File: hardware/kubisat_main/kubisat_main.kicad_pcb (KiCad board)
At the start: 2 copper layers, 80 x 80 mm, 55 parts, among them J1 IPX, J2 Micro_SD_Card_Det1, J3 Conn_01x06_MountingPin, SW1 BOOTSEL, SW2 RESET, U1 RP2040, U2 NEO-6M-GPS, U3 MPU-6050, U4 MMC5883MA, U6 W25Q16JVSS, U6 XL1278-SMT, U7 BME280, U8 DS3231M, Y1 12MHz

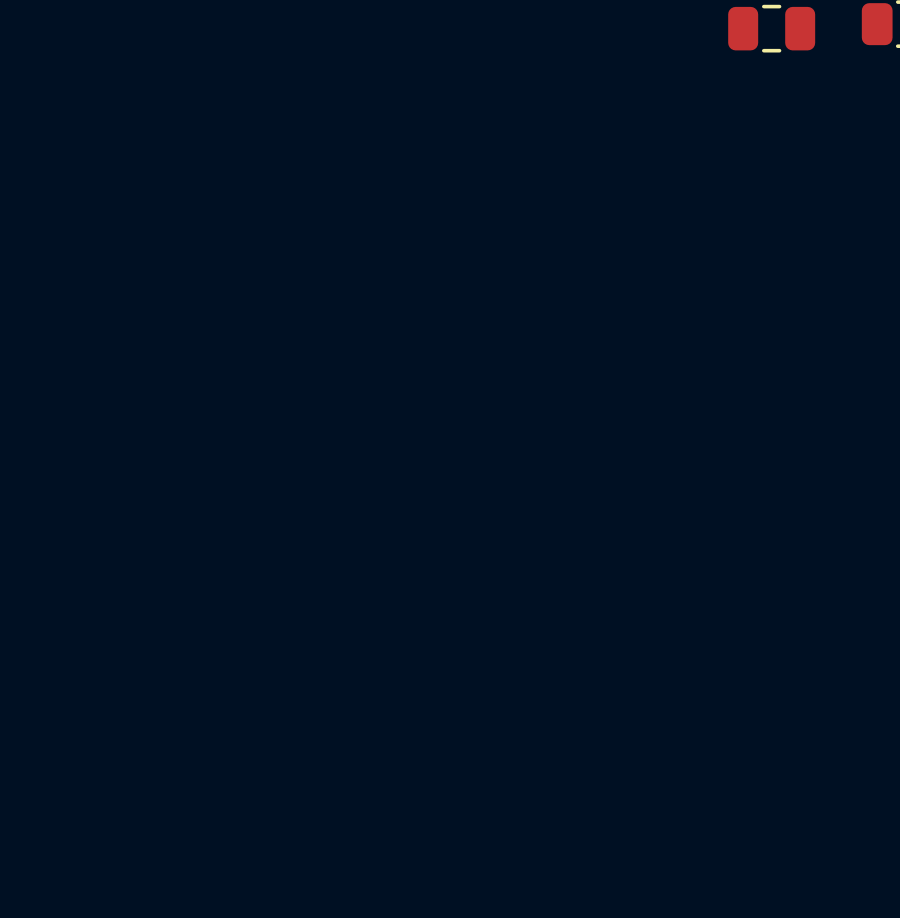
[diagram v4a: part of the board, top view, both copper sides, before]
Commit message: added pcb elements
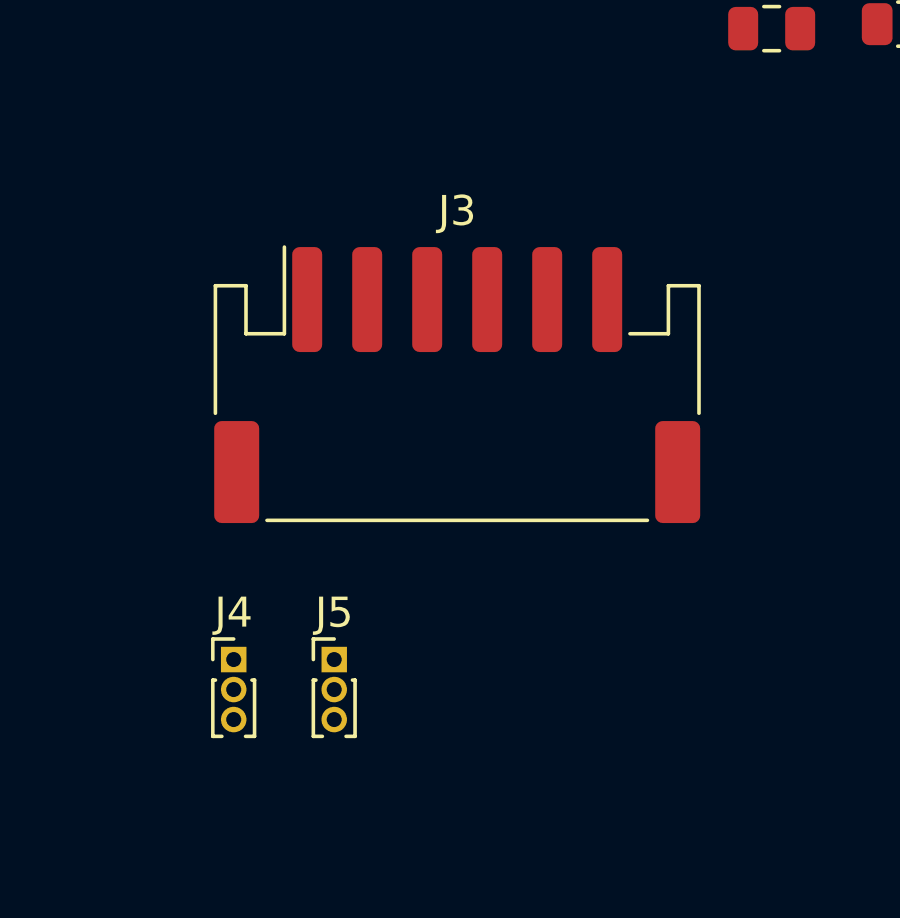
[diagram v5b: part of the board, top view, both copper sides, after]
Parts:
- added J3: Conn_01x06_MountingPin, Connector_JST:JST_PH_S6B-PH-SM4-TB_1x06-1MP_P2.00mm_Horizontal, F.Cu at (47.0, 74.2)
- added J4: DEBUG_SWD, Connector_PinHeader_1.00mm:PinHeader_1x03_P1.00mm_Vertical, F.Cu at (39.5, 83.4)
- added J5: UART0, Connector_PinHeader_1.00mm:PinHeader_1x03_P1.00mm_Vertical, F.Cu at (42.9, 83.4)
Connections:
- U1 pad 2: UART0_TX -> Net-(J5-Pin_3)
- U1 pad 24: unconnected-(U1-SWCLK-Pad24) -> Net-(J4-Pin_1)
- U1 pad 25: unconnected-(U1-SWD-Pad25) -> Net-(J4-Pin_3)
- U1 pad 3: UART0_RX -> Net-(J5-Pin_1)

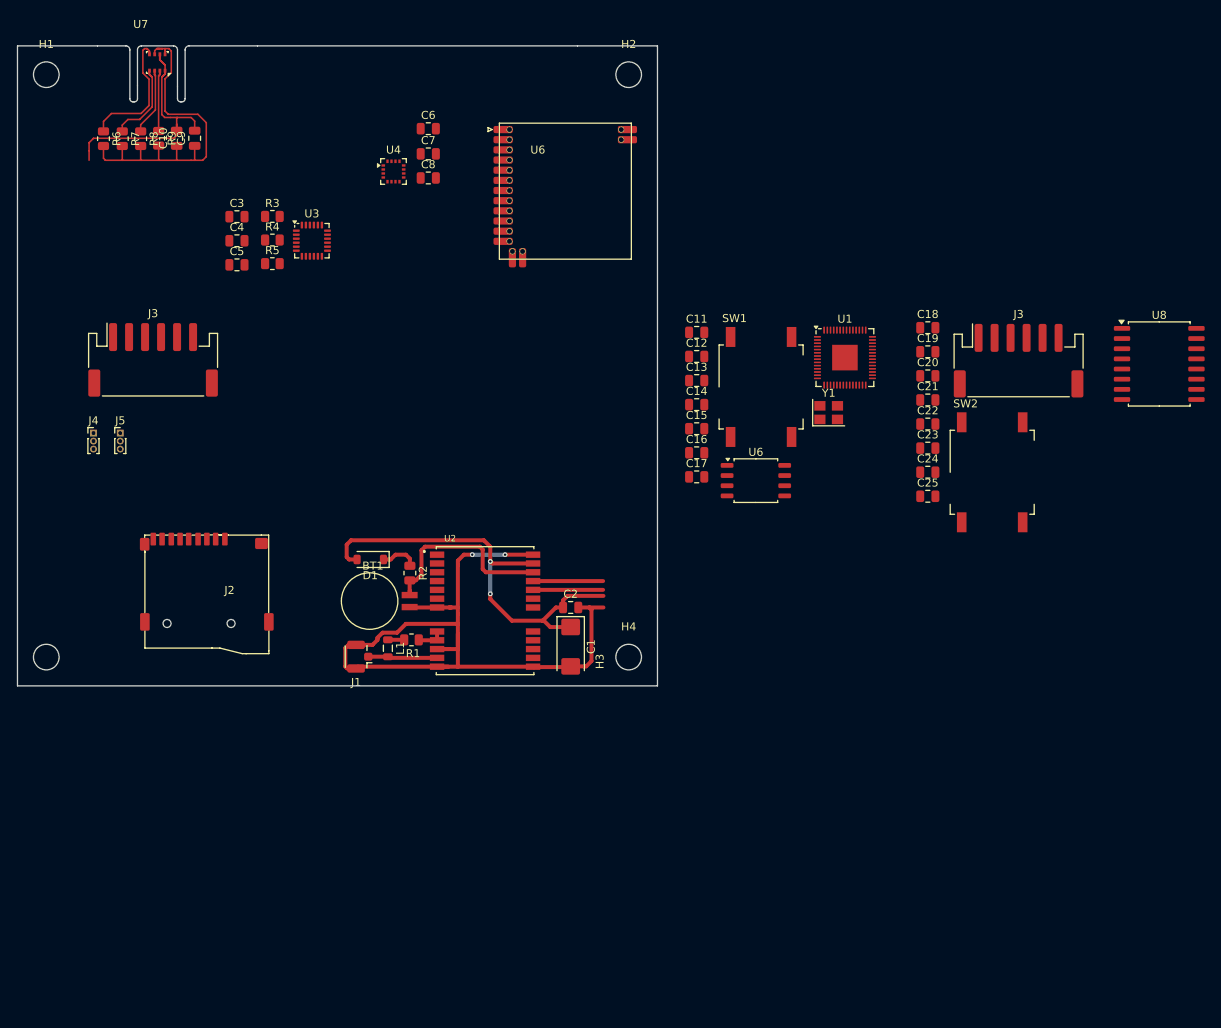
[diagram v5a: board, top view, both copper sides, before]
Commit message: changed strucutre, split main into 2 sseparate boards
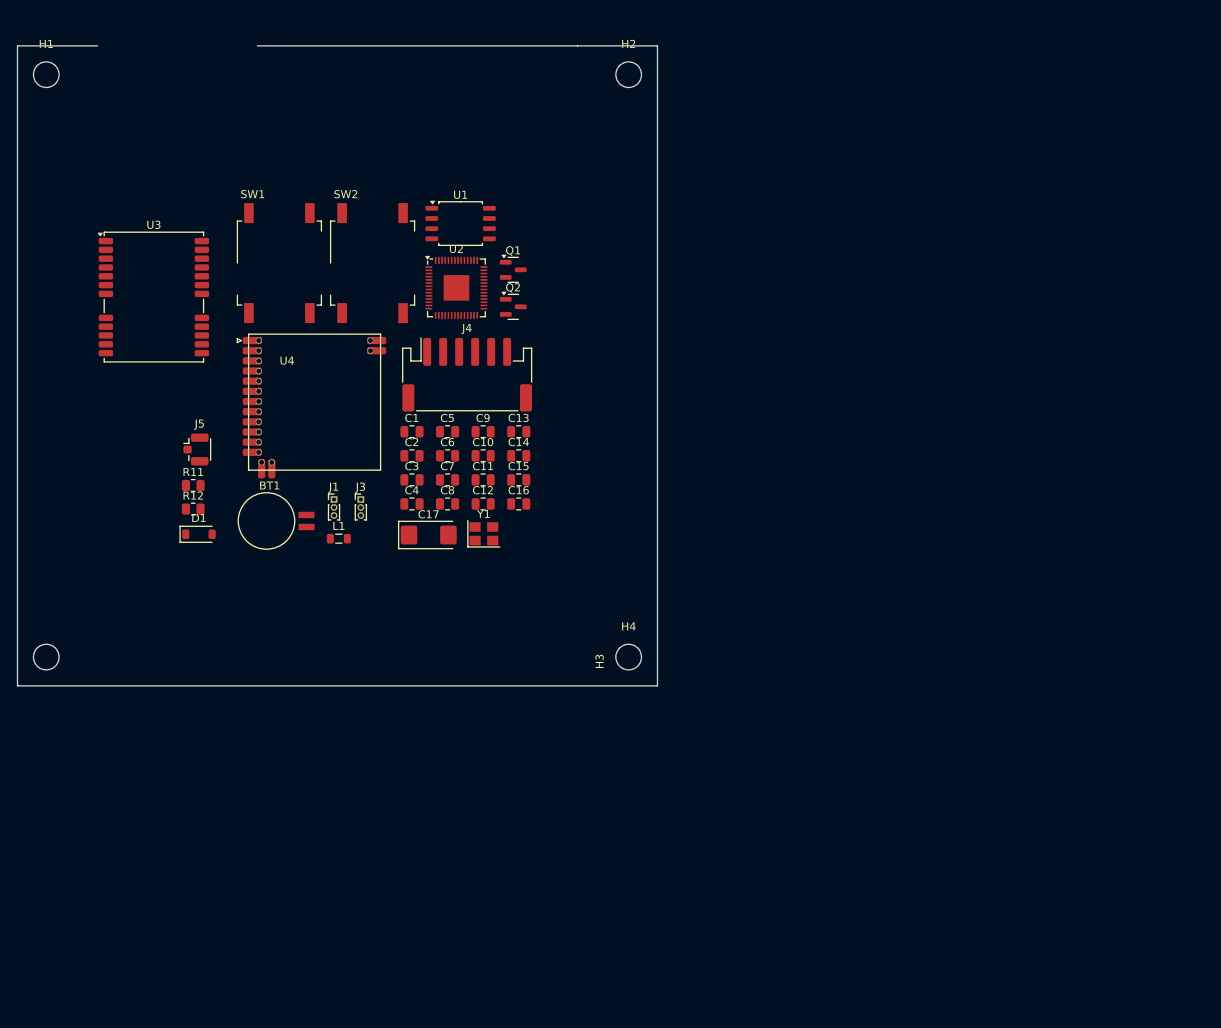
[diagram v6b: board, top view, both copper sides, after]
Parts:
- removed C18, C19, C20, C21, C22, C23, C24, C25: 100n, Capacitor_SMD:C_0805_2012Metric
- removed J2: Micro_SD_Card_Det1, Connector_Card:MR01A-01211
- removed the J3 at (155.1, 74.3)
- removed the J3 at (47.0, 74.2)
- removed R1: 22, Resistor_SMD:R_0805_2012Metric
- removed R2: 1k, Resistor_SMD:R_0805_2012Metric
- removed R3, R4, R5: 4k7, Resistor_SMD:R_0805_2012Metric
- removed R6, R7, R8, R9: 10k, Resistor_SMD:R_0805_2012Metric
- removed U6: W25Q16JVSS, Package_SO:SOIC-8_5.23x5.23mm_P1.27mm
- removed U6: XL1278-SMT, RF:XL1278-SMT
- removed U7: BME280, Package_LGA:Bosch_LGA-8_2.5x2.5mm_P0.65mm_ClockwisePinNumbering
- removed U8: DS3231M, Package_SO:SOIC-16W_7.5x10.3mm_P1.27mm
- added J3: UART0, Connector_PinHeader_1.00mm:PinHeader_1x03_P1.00mm_Vertical, F.Cu at (72.9, 91.7)
- added Q1: BSS138, Package_TO_SOT_SMD:SOT-23, F.Cu at (92.0, 63.0)
- added Q2: BSS138, Package_TO_SOT_SMD:SOT-23, F.Cu at (92.0, 67.6)
- added R11: 22, Resistor_SMD:R_0805_2012Metric, F.Cu at (52.0, 90.0)
- added R12: 1k, Resistor_SMD:R_0805_2012Metric, F.Cu at (52.0, 92.9)
- C1: value 220u/10V -> 100n; footprint Capacitor_Tantalum_SMD:CP_EIA-6032-15_Kemet-U -> Capacitor_SMD:C_0805_2012Metric
- C10: value 1u -> 100n
- C13: value 2u2 -> 100n
- C16: value 15p -> 100n
- C17: value 15p -> 220u/10V; footprint Capacitor_SMD:C_0805_2012Metric -> Capacitor_Tantalum_SMD:CP_EIA-6032-15_Kemet-U
- C4: value 10n -> 100n
- C5: value 2n2 -> 2u2
- C6: value 100n -> 15p
- C7: value 4u7 -> 15p
- C8: value 200n -> 100n
- J1: value IPX -> DEBUG_SWD; footprint Connector_Coaxial:U.FL_Hirose_U.FL-R-SMT-1_Vertical -> Connector_PinHeader_1.00mm:PinHeader_1x03_P1.00mm_Vertical
- J4: value DEBUG_SWD -> POWER_IN; footprint Connector_PinHeader_1.00mm:PinHeader_1x03_P1.00mm_Vertical -> Connector_JST:JST_PH_S6B-PH-SM4-TB_1x06-1MP_P2.00mm_Horizontal
- J5: value UART0 -> IPX; footprint Connector_PinHeader_1.00mm:PinHeader_1x03_P1.00mm_Vertical -> Connector_Coaxial:U.FL_Hirose_U.FL-R-SMT-1_Vertical
- U1: value RP2040 -> W25Q16JVSS; footprint Package_DFN_QFN:QFN-56-1EP_7x7mm_P0.4mm_EP3.2x3.2mm -> Package_SO:SOIC-8_5.23x5.23mm_P1.27mm
- U2: value NEO-6M-GPS -> RP2040; footprint RF_GPS:XCVR_NEO-6M-GPS -> Package_DFN_QFN:QFN-56-1EP_7x7mm_P0.4mm_EP3.2x3.2mm
- U3: value MPU-6050 -> NEO-6M-GPS; footprint Sensor_Motion:InvenSense_QFN-24_4x4mm_P0.5mm -> RF_GPS:ublox_NEO
- U4: value MMC5883MA -> XL1278-SMT; footprint Package_LGA:LGA-16_3x3mm_P0.5mm -> RF:XL1278-SMT
- moved SW2 81.7 mm to (74.4, 62.1)
- moved SW1 62.2 mm to (62.7, 62.1)
- moved C10 55.2 mm to (88.2, 86.2), turned to 0 degrees
- moved C9 51.4 mm to (88.2, 83.2), turned to 0 degrees
- moved U1 50.9 mm to (85.4, 57.2)
- moved J4 47.3 mm to (86.2, 76.1)
- moved Y1 45.7 mm to (88.3, 96.0)
- moved C6 41.0 mm to (83.8, 86.2)
- moved C8 40.8 mm to (83.8, 92.3)
- moved C7 40.8 mm to (83.8, 89.2)
- moved U2 40.5 mm to (84.9, 65.2)
- moved C3 39.5 mm to (79.3, 89.2)
- moved C4 39.5 mm to (79.3, 92.3)
- moved C17 34.3 mm to (81.4, 96.1)
- moved C5 33.6 mm to (83.8, 83.2)
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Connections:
- C1 pad 1: +3V3 -> GND
- C1 pad 2: GND -> +3V3
- C11 pad 1: +1V1 -> +3V3
- C12 pad 1: GND -> +3V3
- C12 pad 2: +1V1 -> GND
- C13 pad 1: GND -> +3V3
- C13 pad 2: Net-(U1-ADC_AVDD) -> GND
- C14 pad 1: GND -> +3V3
- C14 pad 2: +3V3 -> GND
- C15 pad 2: +3V3 -> Net-(U2-ADC_AVDD)
- C16 pad 1: GND -> +3V3
- C16 pad 2: Net-(U1-XIN) -> GND
- C17 pad 1: GND -> +3V3
- C17 pad 2: Net-(C17-Pad2) -> GND
- C2 pad 1: +3V3 -> +1V1
- C3 pad 2: Net-(U3-REGOUT) -> +1V1
- C4 pad 1: +3V3 -> GND
- C4 pad 2: GND -> +1V1
- C5 pad 1: Net-(U3-CPOUT) -> GND
- C5 pad 2: GND -> +3V3
- C6 pad 1: +3V3 -> GND
- C6 pad 2: GND -> Net-(U2-XIN)
- C7 pad 1: unconnected-(C7-Pad1) -> GND
- C7 pad 2: GND -> Net-(C7-Pad2)
- C8 pad 1: unconnected-(C8-Pad1) -> +3V3
- C8 pad 2: unconnected-(C8-Pad2) -> GND
- J1 pad 1: RF_IN -> Net-(J1-Pin_1)
- J4 pad 1: Net-(J4-Pin_1) -> GND
- J4 pad 3: Net-(J4-Pin_3) -> /NC
- J5 pad 1: Net-(J5-Pin_1) -> RF_IN
- SW2 pad 2: Net-(U1-RUN) -> Net-(U2-RUN)
- U1 pad 1: +3V3 -> Net-(U1-~{CS})
- U1 pad 2: Net-(J5-Pin_3) -> Net-(U1-DO(IO1))
- U1 pad 3: Net-(J5-Pin_1) -> Net-(U1-IO2)
- U1 pad 4: unconnected-(U1-GPIO2-Pad4) -> GND
- U1 pad 5: unconnected-(U1-GPIO3-Pad5) -> Net-(U1-DI(IO0))
- U1 pad 6: I2C0_SDA -> Net-(U1-CLK)
- U1 pad 7: I2C0_SCL -> Net-(U1-IO3)
- U1 pad 8: unconnected-(U1-GPIO6-Pad8) -> +3V3
- U2 pad 1: (no net) -> +3V3
- U2 pad 10: GND -> +3V3
- U2 pad 11: RF_IN -> SD.MISO
- U2 pad 12: GND -> SD.CS
- U2 pad 13: GND -> SD.CLK
- U2 pad 14: unconnected-(U2-MOSI/CFG_COM0-Pad14) -> SD.MOSI
- U2 pad 16: unconnected-(U2-CFG_GPS0/SCK-Pad16) -> SX1278.DIO1
- U2 pad 17: unconnected-(U2-RSVD_17-Pad17) -> SX1278.DIO0
- U2 pad 18: unconnected-(U2-SDA2-Pad18) -> SX1278.RES
- U2 pad 19: unconnected-(U2-SCL2-Pad19) -> GND
- U2 pad 2: unconnected-(U2-SS_N-Pad2) -> Net-(J3-Pin_3)
- U2 pad 20: unconnected-(U2-TXD1-Pad20) -> Net-(U2-XIN)
- U2 pad 21: unconnected-(U2-RXD1-Pad21) -> Net-(U2-XOUT)
- U2 pad 22: Net-(BT1-+) -> +3V3
- U2 pad 23: +3V3 -> +1V1
- U2 pad 24: GND -> Net-(J1-Pin_1)
- U2 pad 3: unconnected-(U2-TIMEPULSE-Pad3) -> Net-(J3-Pin_1)
- U2 pad 6: unconnected-(U2-USB_DP-Pad6) -> I2C0_SDA
- U2 pad 7: GND -> I2C0_SCL
- U2 pad 8: Net-(U2-RSVD_8) -> unconnected-(U2-GPIO6-Pad8)
- U2 pad 9: Net-(U2-RSVD_8) -> unconnected-(U2-GPIO7-Pad9)
- U3 pad 1: GND -> (no net)
- U3 pad 10: Net-(U3-REGOUT) -> GND
- U3 pad 11: GND -> RF_IN
- U3 pad 12: unconnected-(U3-INT-Pad12) -> GND
- U3 pad 13: +3V3 -> GND
- U3 pad 18: GND -> unconnected-(U3-SDA2-Pad18)
- U3 pad 20: Net-(U3-CPOUT) -> GPS_TX
- U3 pad 21: unconnected-(U3-RESV-Pad21) -> GPS_RX
- U3 pad 22: unconnected-(U3-RESV-Pad22) -> Net-(BT1-+)
- U3 pad 23: SCL -> +3V3
- U3 pad 24: SDA -> GND
- U3 pad 7: unconnected-(U3-AUX_CL-Pad7) -> GND
- U3 pad 8: +3V3 -> Net-(U3-RSVD_8)
- U3 pad 9: Net-(U3-AD0) -> Net-(U3-RSVD_8)
- U4 pad 1: unconnected-(U4-SCL-Pad1) -> GND
- U4 pad 10: unconnected-(U4-CAP-Pad10) -> /DIO0
- U4 pad 11: Net-(U4-GND-Pad11) -> /RES
- U4 pad 12: unconnected-(U4-NC-Pad12) -> GND
- U4 pad 16: unconnected-(U4-SDA-Pad16) -> Net-(AE1-A)
- U4 pad 2: unconnected-(U4-VDD-Pad2) -> /DIO1
- U4 pad 5: unconnected-(U4-NC-Pad5) -> SX1278_VCC
- U4 pad 6: unconnected-(U4-NC-Pad6) -> /MISO
- U4 pad 7: unconnected-(U4-NC-Pad7) -> /MOSI
- U4 pad 8: unconnected-(U4-NC-Pad8) -> /SCLK
- U4 pad 9: Net-(U4-GND-Pad11) -> /NSS
- Y1 pad 1: Net-(U1-XIN) -> Net-(U2-XIN)
- Y1 pad 3: Net-(C17-Pad2) -> Net-(C7-Pad2)
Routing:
- net GND: track 128.3 -> 0.00 mm, vias 2 -> 0
- net +3V3: track 101.4 -> 0.00 mm, vias 2 -> 0
- net Net-(BT1-+): track 23.6 -> 0.00 mm
- net Net-(U7-SDO): track 17.3 -> 0.00 mm
- net SCL: track 11.2 -> 0.00 mm
- net SDA: track 9.11 -> 0.00 mm
- net unconnected-(U2-TXD1-Pad20): track 8.75 -> 0.00 mm
- net unconnected-(U2-RXD1-Pad21): track 8.75 -> 0.00 mm
- net RF_IN: track 8.66 -> 0.00 mm
- net Net-(U7-CSB): track 8.39 -> 0.00 mm
- net Net-(D1-K): track 4.64 -> 0.00 mm
- net Net-(U2-RSVD_8): track 3.15 -> 0.00 mm
- net Net-(L1-Pad1): track 2.04 -> 0.00 mm
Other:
- outline, holes or cut-outs redrawn

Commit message: completed (?) mainboard schematic
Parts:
- removed C10, C11, C12, C13, C14, C3, C4, C8, C9: 100n, Capacitor_SMD:C_0805_2012Metric
- removed C15, C5: 2u2, Capacitor_SMD:C_0805_2012Metric
- removed C6, C7: 15p, Capacitor_SMD:C_0805_2012Metric
- removed D1: 1N5817, Diode_SMD:D_SOD-123
- removed R12: 1k, Resistor_SMD:R_0805_2012Metric
- removed SW1: BOOTSEL, Button_Switch_SMD:SW_MEC_5GSH9
- removed U2: RP2040, Package_DFN_QFN:QFN-56-1EP_7x7mm_P0.4mm_EP3.2x3.2mm
- removed Y1: 12MHz, Crystal:Crystal_SMD_3225-4Pin_3.2x2.5mm
- added J2: Micro_SD_Card_Det1, Connector_Card:J_SD_Card-micro_socket_A, F.Cu at (68.7, 44.7)
- added J6: POWER, Connector_JST:JST_PH_B3B-PH-SM4-TB_1x03-1MP_P2.00mm_Vertical, F.Cu at (45.0, 110.7)
- added J7: I2C1, Connector_JST:JST_PH_B2B-PH-SM4-TB_1x02-1MP_P2.00mm_Vertical, F.Cu at (56.9, 110.8)
- added J8: SPI0, Connector_JST:JST_PH_B4B-PH-SM4-TB_1x04-1MP_P2.00mm_Vertical, F.Cu at (36.3, 97.1)
- added JP1: ECO, Jumper:SolderJumper-2_P1.3mm_Open_RoundedPad1.0x1.5mm, F.Cu at (59.5, 89.0)
- added R1: 4k7, Resistor_SMD:R_0805_2012Metric, F.Cu at (70.1, 76.7)
- added R10: 10k, Resistor_SMD:R_0805_2012Metric, F.Cu at (66.5, 102.0)
- added R2: 4k7, Resistor_SMD:R_0805_2012Metric, F.Cu at (65.5, 77.0)
- added R3: 4k7, Resistor_SMD:R_0805_2012Metric, F.Cu at (64.8, 56.9)
- added R4: 4k7, Resistor_SMD:R_0805_2012Metric, F.Cu at (67.7, 56.9)
- added R5: 4k7, Resistor_SMD:R_0805_2012Metric, F.Cu at (70.7, 56.9)
- added R6: 4k7, Resistor_SMD:R_0805_2012Metric, F.Cu at (73.6, 56.9)
- added R7: 10k, Resistor_SMD:R_0805_2012Metric, F.Cu at (75.3, 102.0)
- added R8: 10k, Resistor_SMD:R_0805_2012Metric, F.Cu at (72.4, 102.0)
- added R9: 10k, Resistor_SMD:R_0805_2012Metric, F.Cu at (69.5, 102.0)
- added U5: ~, Package_TO_SOT_SMD:SOT-23-5, F.Cu at (47.4, 92.1)
- added U6: Pico, KiCadLibraries:RPi_Pico_SMD_TH, F.Cu at (90.0, 62.2)
- BT1: value Battery_Cell -> LIR2023; footprint Battery:BatteryHolder_Seiko_MS621F -> Battery:BatteryHolder_Keystone_106_1x20mm
- C1, C2: value 100n -> 10u; footprint Capacitor_SMD:C_0805_2012Metric -> Capacitor_Tantalum_SMD:CP_EIA-3216-18_Kemet-A
- SW2: footprint Button_Switch_SMD:SW_MEC_5GSH9 -> Button_Switch_SMD:SW_SPST_B3SL-1002P
- U1: value W25Q16JVSS -> DS3231M; footprint Package_SO:SOIC-8_5.23x5.23mm_P1.27mm -> Package_SO:SOIC-16W_7.5x10.3mm_P1.27mm
- moved BT1 59.8 mm to (45.1, 38.4), turned to -90 degrees
- moved U4 47.9 mm to (100.8, 97.0), turned to -90 degrees
- moved J1 45.2 mm to (107.7, 67.5)
- moved J3 38.9 mm to (107.5, 73.8)
- moved Q1 38.7 mm to (74.0, 97.2), turned to -90 degrees
- moved Q2 37.2 mm to (69.3, 97.2), turned to -90 degrees
- moved J4 36.6 mm to (71.2, 109.5)
- moved SW2 35.3 mm to (109.3, 56.5), turned to -90 degrees
- moved C16 35.3 mm to (57.4, 93.1)
- moved C1 27.0 mm to (56.2, 97.1)
- moved C17 25.5 mm to (59.4, 83.2)
- moved U1 20.5 mm to (67.5, 67.2)
- moved L1 20.1 mm to (53.1, 86.0)
- moved C2 18.2 mm to (62.3, 92.6)
- moved U3 14.6 mm to (41.0, 79.7)
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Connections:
- BT1 pad 1: Net-(BT1-+) -> 3V_BACKUP
- C1 pad 1: GND -> +5V
- C1 pad 2: +3V3 -> GND
- C2 pad 1: +1V1 -> 3V3_GPS
- J3 pad 2: GND -> Net-(J3-Pin_2)
- J3 pad 3: Net-(J3-Pin_3) -> GND
- J4 pad 4: 5VIN -> +5V
- Q1 pad 1: 3V3 -> +3.3V
- Q1 pad 2: I2C0_SCL -> I2C1_SCL
- Q2 pad 1: 3V3 -> +3.3V
- Q2 pad 2: I2C0_SDA -> I2C1_SDA
- SW2 pad 1: GND -> Net-(SW2-Pad1)
- U1 pad 1: Net-(U1-~{CS}) -> unconnected-(U1-32KHZ-Pad1)
- U1 pad 2: Net-(U1-DO(IO1)) -> +3V3
- U1 pad 3: Net-(U1-IO2) -> unconnected-(U1-~{INT}/SQW-Pad3)
- U1 pad 4: GND -> unconnected-(U1-~{RST}-Pad4)
- U1 pad 5: Net-(U1-DI(IO0)) -> GND
- U1 pad 6: Net-(U1-CLK) -> GND
- U1 pad 7: Net-(U1-IO3) -> GND
- U1 pad 8: +3V3 -> GND
- U3 pad 16: unconnected-(U3-CFG_GPS0/SCK-Pad16) -> Net-(JP1-A)
- U3 pad 22: Net-(BT1-+) -> 3V_BACKUP
- U3 pad 23: +3V3 -> 3V3_GPS
- U4 pad 5: SX1278_VCC -> +3.3V
